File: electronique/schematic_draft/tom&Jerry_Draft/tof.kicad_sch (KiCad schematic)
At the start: 7 parts, among them J1201 Conn_02x05_Odd_MALE, J1202 Conn_02x05_Odd_MALE, J1203 Conn_02x05_Odd_FEMALE, J1204 Conn_02x05_Odd_FEMALE, U1202 VL53L1CXV0FY1

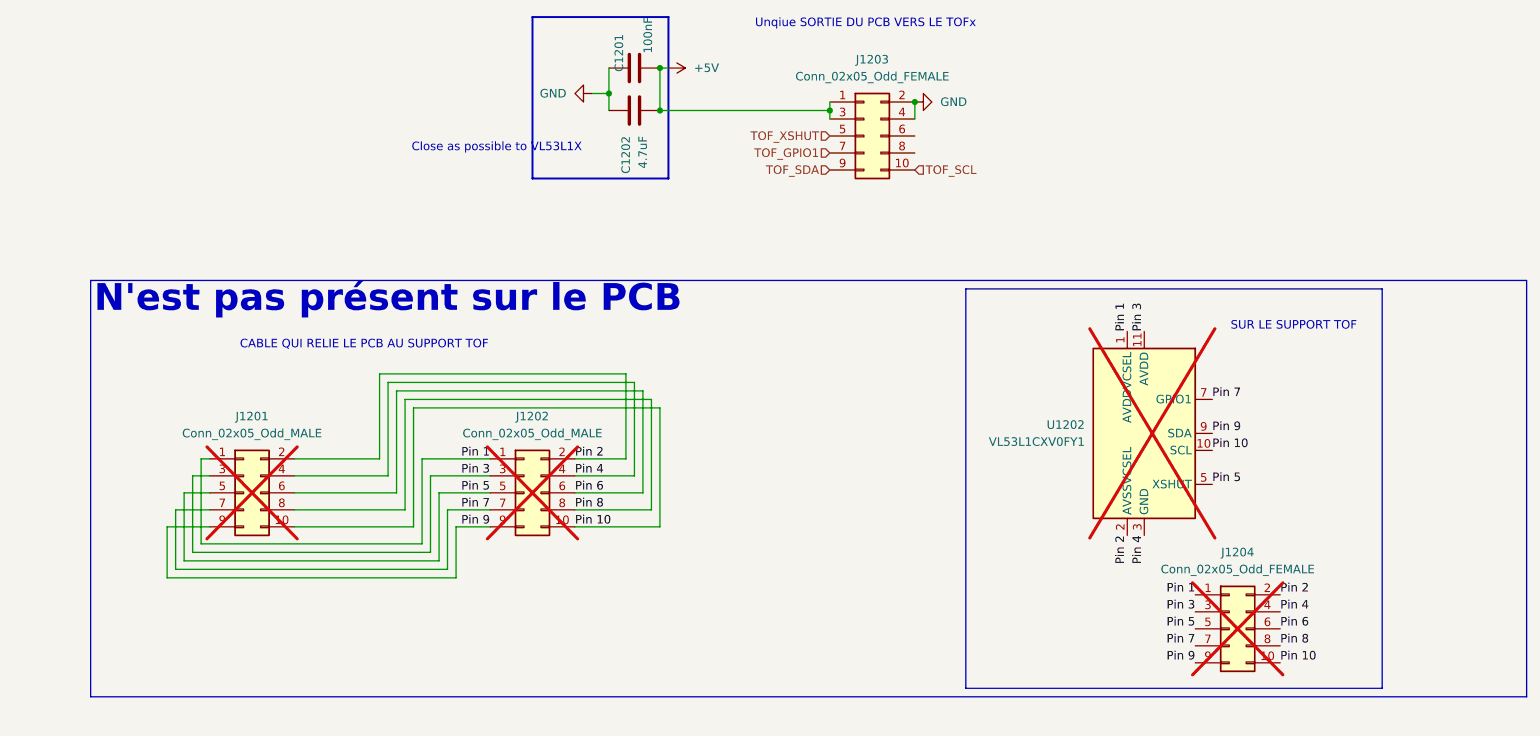
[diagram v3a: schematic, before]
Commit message: STM32 KiCAD v2.0 x CubeIDE - Pin definitif + schematic reviewed
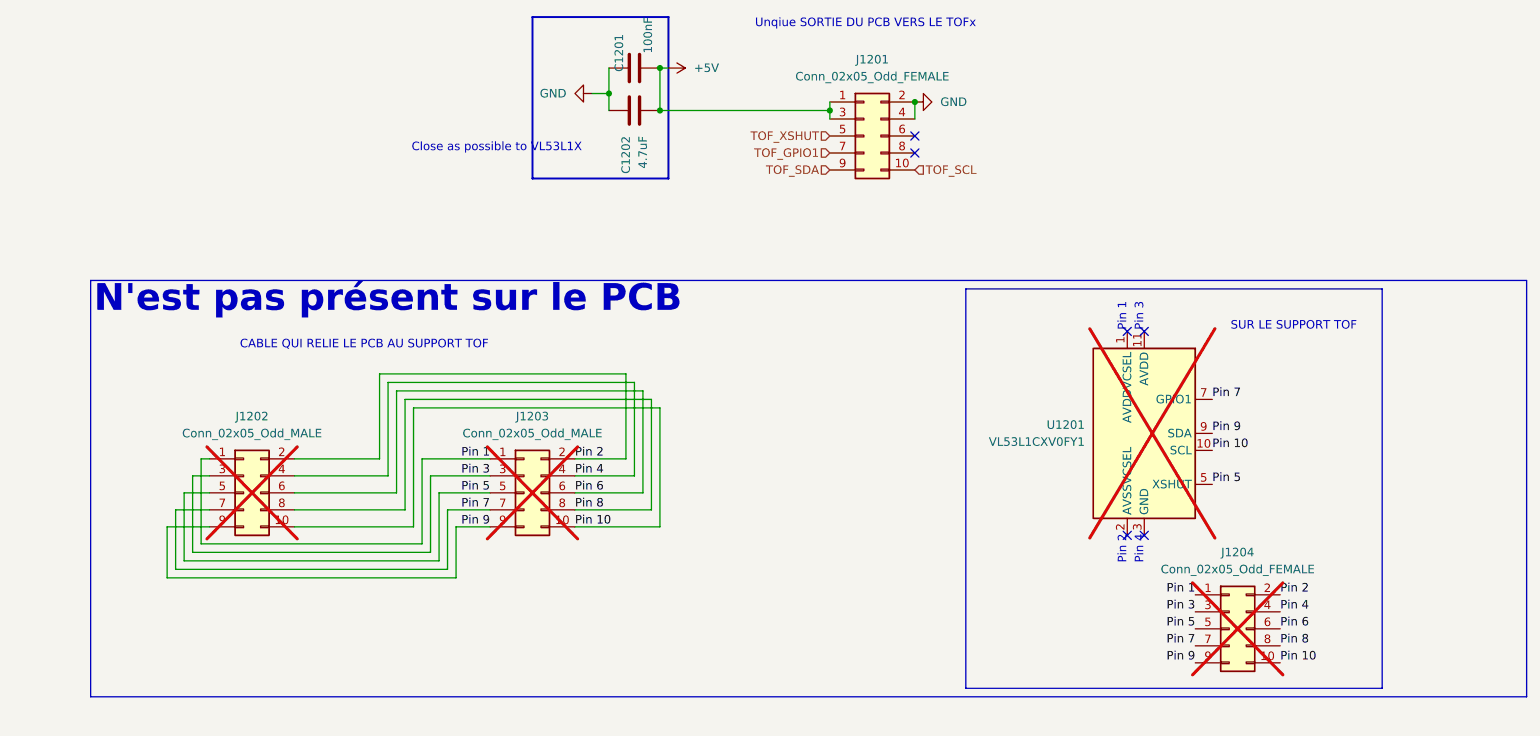
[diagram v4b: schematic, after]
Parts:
- renumbered J1203 to J1201, J1201 to J1202, J1202 to J1203, U1202 to U1201
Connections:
- net Pin 1: no longer U1201.1 (AVDDVCSEL)
- net Pin 2: no longer U1201.2 (AVSSVCSEL)
- net Pin 3: no longer U1201.11 (AVDD)
- net Pin 4: no longer U1201.12 (GND), U1201.3 (GND), U1201.4 (GND), U1201.6 (GND)
- new net: U1201.12 (GND), U1201.3 (GND), U1201.4 (GND), U1201.6 (GND)
- no-connect marks 0 -> 6
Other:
- note added: "Pin 1"
- note added: "Pin 2"
- note added: "Pin 3"
- note added: "Pin 4"
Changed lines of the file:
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@@
 		(color 0 0 0 0)
+	)
+	(no_connect
+		(at 222.25 85.09)
+	)
+	(no_connect
+		(at 190.5 55.88)
+	)
+	(no_connect
+		(at 224.79 115.57)
+	)
+	(no_connect
+		(at 190.5 58.42)
+	)
+	(no_connect
+		(at 224.79 85.09)
+	)
+	(no_connect
+		(at 222.25 115.57)
 	)
 	(wire
@@
 		)
 	)
+	(text "Pin 1"
+		(exclude_from_sim no)
+		(at 222.25 85.09 90)
+		(effects
+			(font
+				(size 1.27 1.27)
+			)
+			(justify left bottom)
+		)
+	)
 	(text "CABLE QUI RELIE LE PCB AU SUPPORT TOF\n"
 		(exclude_from_sim no)
@@
 		)
 	)
+	(text "Pin 2"
+		(exclude_from_sim no)
+		(at 222.25 115.57 90)
+		(effects
+			(font
+				(size 1.27 1.27)
+			)
+			(justify right bottom)
+		)
+	)
+	(text "Pin 4"
+		(exclude_from_sim no)
+		(at 224.79 115.57 90)
+		(effects
+			(font
+				(size 1.27 1.27)
+			)
+			(justify right bottom)
+		)
+	)
 	(text "Unqiue SORTIE DU PCB VERS LE TOFx\n"
 		(exclude_from_sim no)
@@
 		)
 	)
+	(text "Pin 3"
+		(exclude_from_sim no)
+		(at 224.79 85.09 90)
+		(effects
+			(font
+				(size 1.27 1.27)
+			)
+			(justify left bottom)
+		)
+	)
 	(text "N'est pas présent sur le PCB\n"
 		(exclude_from_sim no)
@@
 		)
 	)
-	(label "Pin 3"
-		(at 224.79 85.09 90)
-		(fields_autoplaced yes)
-		(effects
-			(font
-				(size 1.27 1.27)
-			)
-			(justify left bottom)
-		)
-	)
-	(label "Pin 1"
-		(at 222.25 85.09 90)
-		(fields_autoplaced yes)
-		(effects
-			(font
-				(size 1.27 1.27)
-			)
-			(justify left bottom)
-		)
-	)
 	(label "Pin 7"
 		(at 232.41 132.08 180)
@@
 		)
 	)
-	(label "Pin 2"
-		(at 222.25 115.57 270)
-		(fields_autoplaced yes)
-		(effects
-			(font
-				(size 1.27 1.27)
-			)
-			(justify right bottom)
-		)
-	)
 	(label "Pin 9"
 		(at 232.41 134.62 180)
@@
 			)
 			(justify left bottom)
-		)
-	)
-	(label "Pin 4"
-		(at 224.79 115.57 270)
-		(fields_autoplaced yes)
-		(effects
-			(font
-				(size 1.27 1.27)
-			)
-			(justify right bottom)
 		)
 	)
@@
 		(on_board no)
 		(dnp yes)
-		(property "Reference" "U1202"
+		(property "Reference" "U1201"
 			(at 215.9 99.0599 0)
 			(effects
@@
 			(project "tom&Jerry_Draft"
 				(path "/d6e3fbeb-d028-494d-83bf-2e4a8b12578d/ac7f7f04-c418-4551-b204-a999b9c3c440/5425c982-9e7d-49f0-9acd-74ece2531576"
-					(reference "U1202")
+					(reference "U1201")
 					(unit 1)
 				)
 				(path "/d6e3fbeb-d028-494d-83bf-2e4a8b12578d/ac7f7f04-c418-4551-b204-a999b9c3c440/7b81f31a-a9d8-47fc-b567-d77a516e32df"
-					(reference "U1102")
+					(reference "U1101")
 					(unit 1)
 				)
 				(path "/d6e3fbeb-d028-494d-83bf-2e4a8b12578d/ac7f7f04-c418-4551-b204-a999b9c3c440/ae735875-3a05-4be6-99bc-f49af30b564b"
-					(reference "U902")
+					(reference "U901")
 					(unit 1)
 				)
 				(path "/d6e3fbeb-d028-494d-83bf-2e4a8b12578d/ac7f7f04-c418-4551-b204-a999b9c3c440/c40d37b7-0764-4612-8fde-71f5145aa67f"
-					(reference "U802")
+					(reference "U801")
 					(unit 1)
 				)
 				(path "/d6e3fbeb-d028-494d-83bf-2e4a8b12578d/ac7f7f04-c418-4551-b204-a999b9c3c440/d8c0a3ec-14ca-4cad-91fd-ac8f1e686c9a"
-					(reference "U702")
+					(reference "U701")
 					(unit 1)
 				)
 				(path "/d6e3fbeb-d028-494d-83bf-2e4a8b12578d/ac7f7f04-c418-4551-b204-a999b9c3c440/f778e645-32e9-43f1-bc8d-860baaad27c0"
-					(reference "U1002")
+					(reference "U1001")
 					(unit 1)
 				)
@@
 		(dnp no)
 		(fields_autoplaced yes)
-		(property "Reference" "#PWR01204"
+		(property "Reference" "#PWR01203"
 			(at 196.85 50.8 0)
 			(effects
@@
 			(project "tom&Jerry_Draft"
 				(path "/d6e3fbeb-d028-494d-83bf-2e4a8b12578d/ac7f7f04-c418-4551-b204-a999b9c3c440/5425c982-9e7d-49f0-9acd-74ece2531576"
-					(reference "#PWR01204")
+					(reference "#PWR01203")
 					(unit 1)
 				)
 				(path "/d6e3fbeb-d028-494d-83bf-2e4a8b12578d/ac7f7f04-c418-4551-b204-a999b9c3c440/7b81f31a-a9d8-47fc-b567-d77a516e32df"
-					(reference "#PWR01104")
+					(reference "#PWR01103")
 					(unit 1)
 				)
 				(path "/d6e3fbeb-d028-494d-83bf-2e4a8b12578d/ac7f7f04-c418-4551-b204-a999b9c3c440/ae735875-3a05-4be6-99bc-f49af30b564b"
-					(reference "#PWR0904")
+					(reference "#PWR0903")
 					(unit 1)
 				)
 				(path "/d6e3fbeb-d028-494d-83bf-2e4a8b12578d/ac7f7f04-c418-4551-b204-a999b9c3c440/c40d37b7-0764-4612-8fde-71f5145aa67f"
-					(reference "#PWR0804")
+					(reference "#PWR0803")
 					(unit 1)
 				)
 				(path "/d6e3fbeb-d028-494d-83bf-2e4a8b12578d/ac7f7f04-c418-4551-b204-a999b9c3c440/d8c0a3ec-14ca-4cad-91fd-ac8f1e686c9a"
-					(reference "#PWR0704")
+					(reference "#PWR0703")
 					(unit 1)
 				)
 				(path "/d6e3fbeb-d028-494d-83bf-2e4a8b12578d/ac7f7f04-c418-4551-b204-a999b9c3c440/f778e645-32e9-43f1-bc8d-860baaad27c0"
-					(reference "#PWR01004")
+					(reference "#PWR01003")
 					(unit 1)
 				)
@@
 		(on_board yes)
 		(dnp no)
-		(property "Reference" "J1203"
+		(property "Reference" "J1201"
 			(at 184.15 44.45 0)
 			(effects
@@
 			(project "tom&Jerry_Draft"
 				(path "/d6e3fbeb-d028-494d-83bf-2e4a8b12578d/ac7f7f04-c418-4551-b204-a999b9c3c440/5425c982-9e7d-49f0-9acd-74ece2531576"
-					(reference "J1203")
+					(reference "J1201")
 					(unit 1)
 				)
 				(path "/d6e3fbeb-d028-494d-83bf-2e4a8b12578d/ac7f7f04-c418-4551-b204-a999b9c3c440/7b81f31a-a9d8-47fc-b567-d77a516e32df"
-					(reference "J1103")
+					(reference "J1101")
 					(unit 1)
 				)
 				(path "/d6e3fbeb-d028-494d-83bf-2e4a8b12578d/ac7f7f04-c418-4551-b204-a999b9c3c440/ae735875-3a05-4be6-99bc-f49af30b564b"
-					(reference "J903")
+					(reference "J901")
 					(unit 1)
 				)
 				(path "/d6e3fbeb-d028-494d-83bf-2e4a8b12578d/ac7f7f04-c418-4551-b204-a999b9c3c440/c40d37b7-0764-4612-8fde-71f5145aa67f"
-					(reference "J803")
+					(reference "J801")
 					(unit 1)
 				)
 				(path "/d6e3fbeb-d028-494d-83bf-2e4a8b12578d/ac7f7f04-c418-4551-b204-a999b9c3c440/d8c0a3ec-14ca-4cad-91fd-ac8f1e686c9a"
-					(reference "J703")
+					(reference "J701")
 					(unit 1)
 				)
 				(path "/d6e3fbeb-d028-494d-83bf-2e4a8b12578d/ac7f7f04-c418-4551-b204-a999b9c3c440/f778e645-32e9-43f1-bc8d-860baaad27c0"
-					(reference "J1003")
+					(reference "J1001")
 					(unit 1)
 				)
@@
 		(on_board no)
 		(dnp yes)
-		(property "Reference" "J1202"
+		(property "Reference" "J1203"
 			(at 133.35 97.79 0)
 			(effects
@@
 			(project "tom&Jerry_Draft"
 				(path "/d6e3fbeb-d028-494d-83bf-2e4a8b12578d/ac7f7f04-c418-4551-b204-a999b9c3c440/5425c982-9e7d-49f0-9acd-74ece2531576"
-					(reference "J1202")
+					(reference "J1203")
 					(unit 1)
 				)
 				(path "/d6e3fbeb-d028-494d-83bf-2e4a8b12578d/ac7f7f04-c418-4551-b204-a999b9c3c440/7b81f31a-a9d8-47fc-b567-d77a516e32df"
-					(reference "J1102")
+					(reference "J1103")
 					(unit 1)
 				)
 				(path "/d6e3fbeb-d028-494d-83bf-2e4a8b12578d/ac7f7f04-c418-4551-b204-a999b9c3c440/ae735875-3a05-4be6-99bc-f49af30b564b"
-					(reference "J902")
+					(reference "J903")
 					(unit 1)
 				)
 				(path "/d6e3fbeb-d028-494d-83bf-2e4a8b12578d/ac7f7f04-c418-4551-b204-a999b9c3c440/c40d37b7-0764-4612-8fde-71f5145aa67f"
-					(reference "J802")
+					(reference "J803")
 					(unit 1)
 				)
 				(path "/d6e3fbeb-d028-494d-83bf-2e4a8b12578d/ac7f7f04-c418-4551-b204-a999b9c3c440/d8c0a3ec-14ca-4cad-91fd-ac8f1e686c9a"
-					(reference "J702")
+					(reference "J703")
 					(unit 1)
 				)
 				(path "/d6e3fbeb-d028-494d-83bf-2e4a8b12578d/ac7f7f04-c418-4551-b204-a999b9c3c440/f778e645-32e9-43f1-bc8d-860baaad27c0"
-					(reference "J1002")
+					(reference "J1003")
 					(unit 1)
 				)
@@
 		(on_board no)
 		(dnp yes)
-		(property "Reference" "J1201"
+		(property "Reference" "J1202"
 			(at 91.44 97.79 0)
 			(effects
@@
 			(project "tom&Jerry_Draft"
 				(path "/d6e3fbeb-d028-494d-83bf-2e4a8b12578d/ac7f7f04-c418-4551-b204-a999b9c3c440/5425c982-9e7d-49f0-9acd-74ece2531576"
-					(reference "J1201")
+					(reference "J1202")
 					(unit 1)
 				)
 				(path "/d6e3fbeb-d028-494d-83bf-2e4a8b12578d/ac7f7f04-c418-4551-b204-a999b9c3c440/7b81f31a-a9d8-47fc-b567-d77a516e32df"
-					(reference "J1101")
+					(reference "J1102")
 					(unit 1)
 				)
 				(path "/d6e3fbeb-d028-494d-83bf-2e4a8b12578d/ac7f7f04-c418-4551-b204-a999b9c3c440/ae735875-3a05-4be6-99bc-f49af30b564b"
-					(reference "J901")
+					(reference "J902")
 					(unit 1)
 				)
 				(path "/d6e3fbeb-d028-494d-83bf-2e4a8b12578d/ac7f7f04-c418-4551-b204-a999b9c3c440/c40d37b7-0764-4612-8fde-71f5145aa67f"
-					(reference "J801")
+					(reference "J802")
 					(unit 1)
 				)
 				(path "/d6e3fbeb-d028-494d-83bf-2e4a8b12578d/ac7f7f04-c418-4551-b204-a999b9c3c440/d8c0a3ec-14ca-4cad-91fd-ac8f1e686c9a"
-					(reference "J701")
+					(reference "J702")
 					(unit 1)
 				)
 				(path "/d6e3fbeb-d028-494d-83bf-2e4a8b12578d/ac7f7f04-c418-4551-b204-a999b9c3c440/f778e645-32e9-43f1-bc8d-860baaad27c0"
-					(reference "J1001")
-					(unit 1)
-				)
+					(reference "J1002")
+					(unit 1)
+				)

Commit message: Adding footprint V0.1
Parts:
- C1201: footprint (none) -> Capacitor_SMD:C_0402_1005Metric
- C1202: footprint (none) -> Capacitor_SMD:C_0603_1608Metric
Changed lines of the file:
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@@
 			)
 		)
-		(property "Footprint" ""
+		(property "Footprint" "Capacitor_SMD:C_0603_1608Metric"
 			(at 152.4 53.0352 0)
 			(effects
@@
 			)
 		)
-		(property "Footprint" ""
+		(property "Footprint" "Capacitor_SMD:C_0402_1005Metric"
 			(at 152.4 46.6852 0)
 			(effects

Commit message: Changing footprint V0.2
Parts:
- J1201: footprint (none) -> Connector_PinSocket_1.27mm:PinSocket_2x05_P1.27mm_Vertical
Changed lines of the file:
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@@
 			)
 		)
-		(property "Footprint" ""
+		(property "Footprint" "Connector_PinSocket_1.27mm:PinSocket_2x05_P1.27mm_Vertical"
 			(at 182.88 55.88 0)
 			(effects

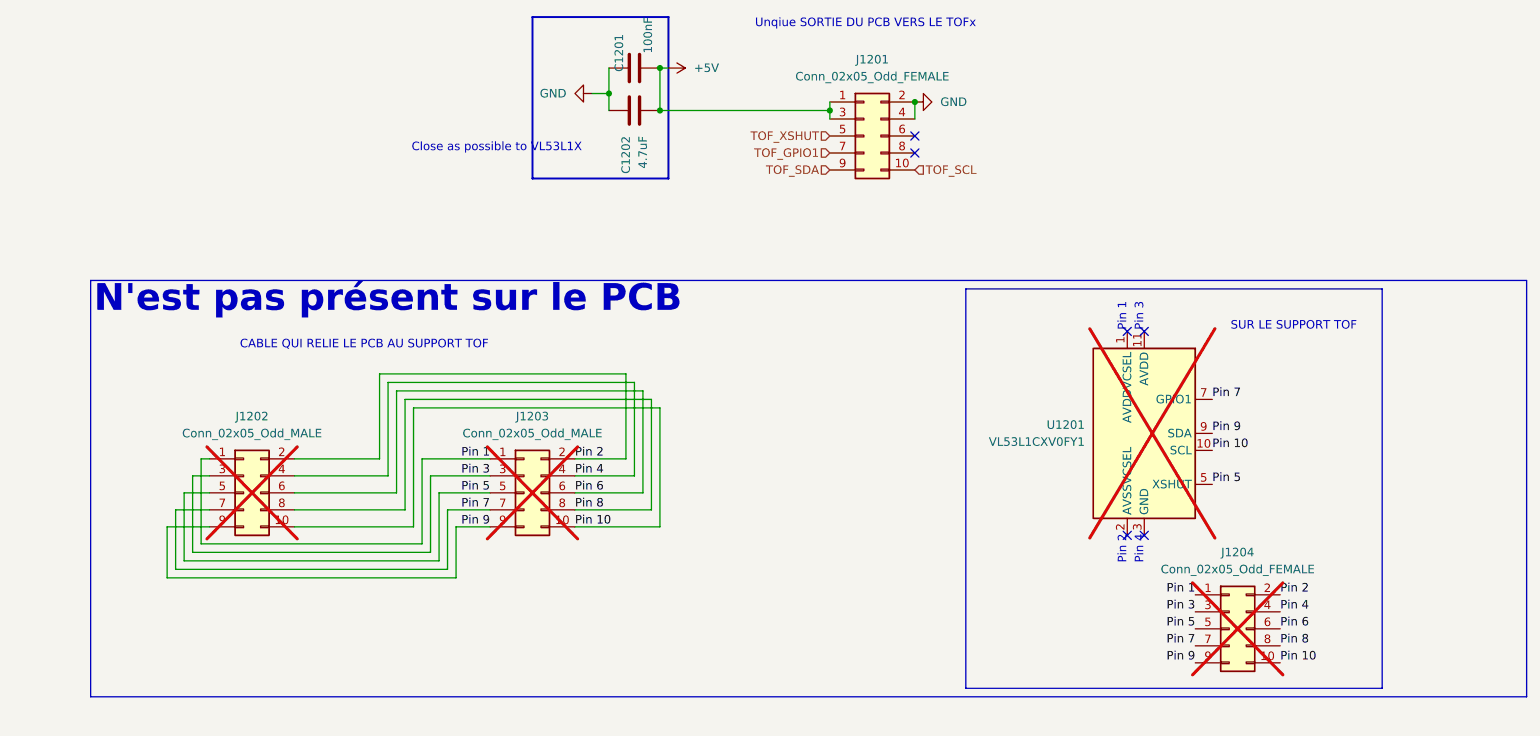
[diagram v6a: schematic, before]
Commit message: Ajout V2 TOF + MultiPCB Panalize
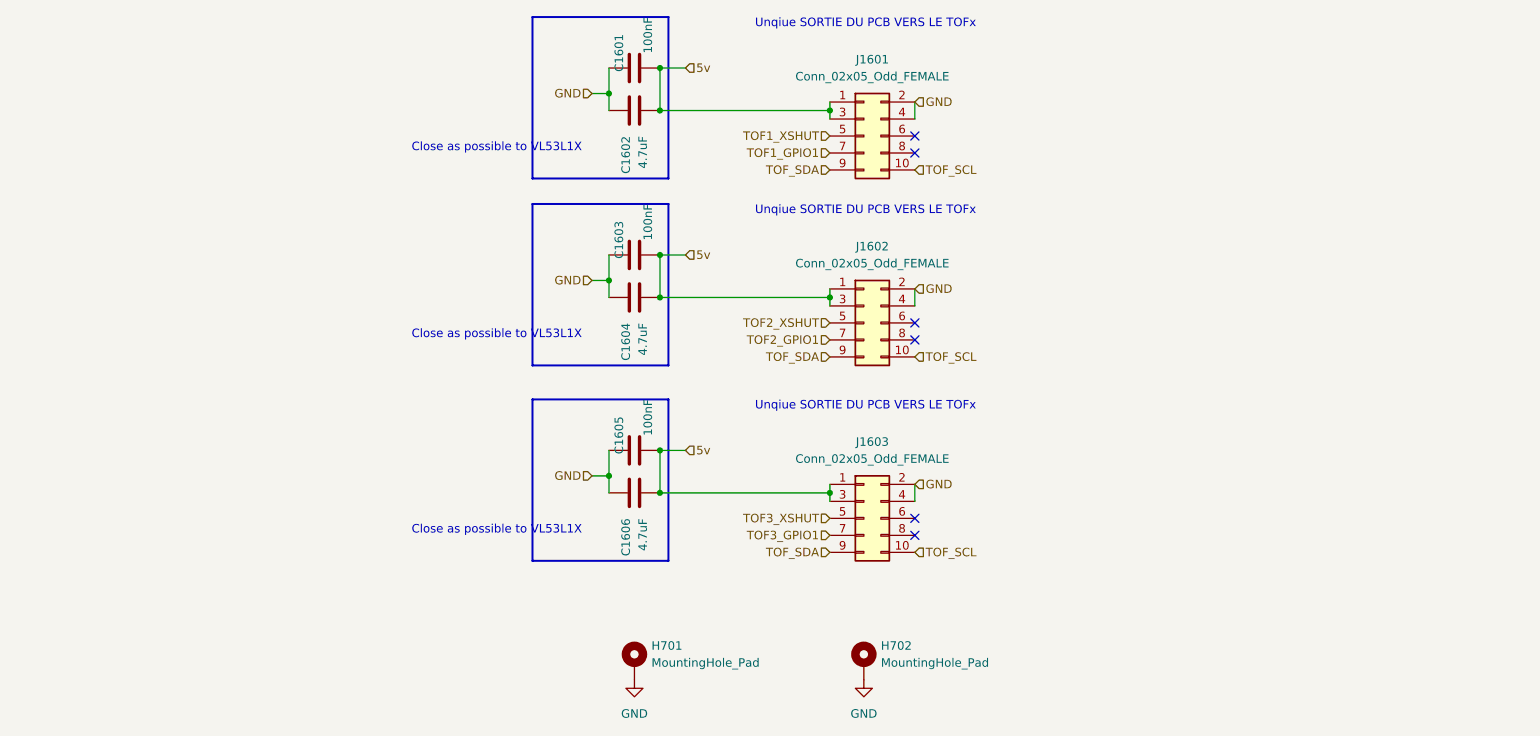
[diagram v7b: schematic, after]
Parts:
- removed J1202, J1203: Conn_02x05_Odd_MALE, symbol Connector_Generic:Conn_02x05_Odd_Even
- removed J1204: Conn_02x05_Odd_FEMALE, symbol Connector_Generic:Conn_02x05_Odd_Even
- removed U1201: VL53L1CXV0FY1, Sensor_Distance:ST_VL53L1x, symbol Sensor_Distance:VL53L1CXV0FY1
- added C1603, C1605: 100nF, Capacitor_SMD:C_0402_1005Metric, symbol Device:C
- added C1604, C1606: 4.7uF, Capacitor_SMD:C_0603_1608Metric, symbol Device:C
- added H701, H702: MountingHole_Pad, MountingHole:MountingHole_3.2mm_M3_Pad_Via, symbol Mechanical:MountingHole_Pad
- added J1602, J1603: Conn_02x05_Odd_FEMALE, Connector_PinSocket_1.27mm:PinSocket_2x05_P1.27mm_Vertical, symbol Connector_Generic:Conn_02x05_Odd_Even
- renumbered C1201 to C1601, C1202 to C1602, J1201 to J1601
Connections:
- net GND: now also C1603.1, C1604.1, C1605.1, C1606.1, H701.1, H702.1, J1602.2 (Pin_2), J1602.4 (Pin_4), J1603.2 (Pin_2), J1603.4 (Pin_4)
- net TOF_SCL: now also J1602.10 (Pin_10), J1603.10 (Pin_10)
- net TOF_SDA: now also J1602.9 (Pin_9), J1603.9 (Pin_9)
- net +5V renamed 5v
- net 5v: now also C1603.2, C1604.2, C1605.2, C1606.2, J1602.1 (Pin_1), J1602.3 (Pin_3), J1603.1 (Pin_1), J1603.3 (Pin_3)
- net TOF_GPIO1 renamed TOF1_GPIO1
- net TOF_XSHUT renamed TOF1_XSHUT
- new net TOF2_GPIO1: J1602.7 (Pin_7)
- new net TOF2_XSHUT: J1602.5 (Pin_5)
- new net TOF3_GPIO1: J1603.7 (Pin_7)
- new net TOF3_XSHUT: J1603.5 (Pin_5)
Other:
- note removed: "CABLE QUI RELIE LE PCB AU SUPPORT TOF"
- note removed: "N'est pas présent sur le PCB"
- note removed: "Pin 1"
- note removed: "Pin 2"
- note removed: "Pin 3"
- note removed: "Pin 4"
- note removed: "SUR LE SUPPORT TOF"

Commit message: Try some placement and routing
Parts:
- renumbered C1601 to C701, C1602 to C702, C1603 to C703, C1604 to C704, C1605 to C705, C1606 to C706, J1601 to J701, J1602 to J702, J1603 to J703
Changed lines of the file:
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@@
 		(on_board yes)
 		(dnp no)
-		(property "Reference" "J1601"
+		(property "Reference" "J701"
 			(at 184.15 44.45 0)
 			(effects
@@
 		(on_board yes)
 		(dnp no)
-		(property "Reference" "C1603"
+		(property "Reference" "C703"
 			(at 146.304 68.58 0)
 			(effects
@@
 		(dnp no)
 		(fields_autoplaced yes)
-		(property "Reference" "C1602"
+		(property "Reference" "C702"
 			(at 147.3199 55.88 0)
 			(effects
@@
 		(dnp no)
 		(fields_autoplaced yes)
-		(property "Reference" "C1606"
+		(property "Reference" "C706"
 			(at 147.3199 113.03 0)
 			(effects
@@
 		(on_board yes)
 		(dnp no)
-		(property "Reference" "J1603"
+		(property "Reference" "J703"
 			(at 184.15 101.6 0)
 			(effects
@@
 		(dnp no)
 		(fields_autoplaced yes)
-		(property "Reference" "C1604"
+		(property "Reference" "C704"
 			(at 147.3199 83.82 0)
 			(effects
@@
 		(on_board yes)
 		(dnp no)
-		(property "Reference" "C1605"
+		(property "Reference" "C705"
 			(at 146.304 97.79 0)
 			(effects
@@
 		(on_board yes)
 		(dnp no)
-		(property "Reference" "J1602"
+		(property "Reference" "J702"
 			(at 184.15 72.39 0)
 			(effects
@@
 		(on_board yes)
 		(dnp no)
-		(property "Reference" "C1601"
+		(property "Reference" "C701"
 			(at 146.304 40.64 0)
 			(effects
